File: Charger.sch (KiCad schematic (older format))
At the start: 47 parts, among them J1 Input, J2 USB-A-S-X-X-SM2, J3 USB-A-S-X-X-SM2, U1 LT1085-5.0, U2 TPS2546, U3 LT3798MPMSETRPBF, U4 TPS2546RTER

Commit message: schematics completed
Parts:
- removed D? (x2): D, symbol Device:D
- removed TR1: TEZ6.0-D-1, Transformer_THT:Transformer_Breve_TEZ-38x45, symbol Transformer:TEZ6.0-D-1
- removed U3: LT3798MPMSETRPBF, MSOP-16_MSE, symbol Charger-rescue:LT3798MPMSETRPBF-LT3798MPMSETRPBF
- added U3: LT3798MPMSETRPBF, MSOP-16_MSE, symbol LT3798MPMSETRPBF:LT3798MPMSETRPBF
- C6: renamed from C?; value C -> 4.7u
- R2: footprint R100k:RESC1005X40N -> (none)
- gave numbers to parts that had none: 28
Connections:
- net labels removed: +, -, DM, DP, Vout
- wire segments 103 -> 107
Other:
- moved on the sheet: D2

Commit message: Update Charger.sch
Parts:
- D4: value D_Zener -> DFLZ33
- D5: value DIODE -> GSD2004W-V
- M1: value MNMOS -> BSC42DN25NS3
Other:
- moved on the sheet: J2, J3
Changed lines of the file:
@@
 L Charger-rescue:USB-A-S-X-X-SM2-USB-A-S-X-X-SM2 J2
 U 1 1 6032BA44
-P 9500 1450
-F 0 "J2" H 9730 1446 50  0000 L CNN
-F 1 "USB-A-S-X-X-SM2" H 9730 1355 50  0000 L CNN
-F 2 "USB:SAMTEC_USB-A-S-X-X-SM2" H 9500 1450 50  0001 L BNN
-F 3 "" H 9500 1450 50  0001 L BNN
-F 4 "7.8 mm" H 9500 1450 50  0001 L BNN "MAXIMUM_PACKAGE_HEIGHT"
-F 5 "T" H 9500 1450 50  0001 L BNN "PARTREV"
-F 6 "Manufacturer Recommendations" H 9500 1450 50  0001 L BNN "STANDARD"
-F 7 "Samtec" H 9500 1450 50  0001 L BNN "MANUFACTURER"
-	1    9500 1450
+P 9600 1000
+F 0 "J2" H 9830 996 50  0000 L CNN
+F 1 "USB-A-S-X-X-SM2" H 9830 905 50  0000 L CNN
+F 2 "USB:SAMTEC_USB-A-S-X-X-SM2" H 9600 1000 50  0001 L BNN
+F 3 "" H 9600 1000 50  0001 L BNN
+F 4 "7.8 mm" H 9600 1000 50  0001 L BNN "MAXIMUM_PACKAGE_HEIGHT"
+F 5 "T" H 9600 1000 50  0001 L BNN "PARTREV"
+F 6 "Manufacturer Recommendations" H 9600 1000 50  0001 L BNN "STANDARD"
+F 7 "Samtec" H 9600 1000 50  0001 L BNN "MANUFACTURER"
+	1    9600 1000
 	1    0    0    -1
 $EndComp
 Text GLabel 6600 4300 3    50   Input ~ 0
 gnd
-Text GLabel 9100 1250 0    50   Input ~ 0
+Text GLabel 9200 800  0    50   Input ~ 0
 Vout1
-Text GLabel 9100 1550 0    50   Input ~ 0
+Text GLabel 9200 1100 0    50   Input ~ 0
 gnd
 $Comp
@@
 	1    0    0    -1
 $EndComp
-Text GLabel 9100 1350 0    50   Input ~ 0
+Text GLabel 9200 900  0    50   Input ~ 0
 DM1
-Text GLabel 9100 1450 0    50   Input ~ 0
+Text GLabel 9200 1000 0    50   Input ~ 0
 DP1
 Text GLabel 8650 2550 2    50   Input ~ 0
@@
 L Charger-rescue:USB-A-S-X-X-SM2-USB-A-S-X-X-SM2 J3
 U 1 1 60370EEE
-P 9900 4750
-F 0 "J3" H 10130 4746 50  0000 L CNN
-F 1 "USB-A-S-X-X-SM2" H 10130 4655 50  0000 L CNN
-F 2 "SAMTEC_USB-A-S-X-X-SM2" H 9900 4750 50  0001 L BNN
-F 3 "" H 9900 4750 50  0001 L BNN
-F 4 "7.8 mm" H 9900 4750 50  0001 L BNN "MAXIMUM_PACKAGE_HEIGHT"
-F 5 "T" H 9900 4750 50  0001 L BNN "PARTREV"
-F 6 "Manufacturer Recommendations" H 9900 4750 50  0001 L BNN "STANDARD"
-F 7 "Samtec" H 9900 4750 50  0001 L BNN "MANUFACTURER"
-	1    9900 4750
-	1    0    0    -1
-$EndComp
-Text GLabel 9500 4850 0    50   Input ~ 0
-gnd
-Text GLabel 9500 4750 0    50   Input ~ 0
+P 7550 950
+F 0 "J3" H 7780 946 50  0000 L CNN
+F 1 "USB-A-S-X-X-SM2" H 7780 855 50  0000 L CNN
+F 2 "SAMTEC_USB-A-S-X-X-SM2" H 7550 950 50  0001 L BNN
+F 3 "" H 7550 950 50  0001 L BNN
+F 4 "7.8 mm" H 7550 950 50  0001 L BNN "MAXIMUM_PACKAGE_HEIGHT"
+F 5 "T" H 7550 950 50  0001 L BNN "PARTREV"
+F 6 "Manufacturer Recommendations" H 7550 950 50  0001 L BNN "STANDARD"
+F 7 "Samtec" H 7550 950 50  0001 L BNN "MANUFACTURER"
+	1    7550 950
+	1    0    0    -1
+$EndComp
+Text GLabel 7150 1050 0    50   Input ~ 0
+gnd
+Text GLabel 7150 950  0    50   Input ~ 0
 DP2
-Text GLabel 9500 4650 0    50   Input ~ 0
+Text GLabel 7150 850  0    50   Input ~ 0
 DM2
-Text GLabel 9500 4550 0    50   Input ~ 0
+Text GLabel 7150 750  0    50   Input ~ 0
 Vout2
 Text GLabel 8600 4650 2    50   Input ~ 0
@@
 P 5650 5850
 F 0 "M1" H 5938 5896 50  0000 L CNN
-F 1 "MNMOS" H 5938 5805 50  0000 L CNN
+F 1 "BSC42DN25NS3" H 5938 5805 50  0000 L CNN
 F 2 "" H 5625 5850 50  0001 C CNN
 F 3 "~" H 5625 5850 50  0001 C CNN
@@
 P 4600 4700
 F 0 "D5" V 4646 4572 50  0000 R CNN
-F 1 "DIODE" V 4555 4572 50  0000 R CNN
+F 1 "GSD2004W-V" V 4555 4572 50  0000 R CNN
 F 2 "" H 4600 4700 50  0001 C CNN
 F 3 "~" H 4600 4700 50  0001 C CNN
@@
 P 4600 4050
 F 0 "D4" V 4646 3970 50  0000 R CNN
-F 1 "D_Zener" V 4555 3970 50  0000 R CNN
+F 1 "DFLZ33" V 4555 3970 50  0000 R CNN
 F 2 "" H 4600 4050 50  0001 C CNN
 F 3 "~" H 4600 4050 50  0001 C CNN
@@
 L power:PWR_FLAG #FLG0102
 U 1 1 60397240
-P 9100 1550
-F 0 "#FLG0102" H 9100 1625 50  0001 C CNN
-F 1 "PWR_FLAG" H 9100 1723 50  0000 C CNN
-F 2 "" H 9100 1550 50  0001 C CNN
-F 3 "~" H 9100 1550 50  0001 C CNN
-	1    9100 1550
+P 9200 1100
+F 0 "#FLG0102" H 9200 1175 50  0001 C CNN
+F 1 "PWR_FLAG" H 9200 1273 50  0000 C CNN
+F 2 "" H 9200 1100 50  0001 C CNN
+F 3 "~" H 9200 1100 50  0001 C CNN
+	1    9200 1100
 	-1   0    0    1
 $EndComp

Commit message: footprint added
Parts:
- removed D3: 1N4148, symbol Charger-rescue:1N4148-1N4148
- removed L1, L2, L3: L, symbol Device:L
- removed M1: BSC42DN25NS3, symbol pspice:MNMOS
- added D3: 1N4148WS, 1N4148WS:SODFL2512X100N, symbol 1N4148WS:1N4148WS
- added Q1: BSC42DN25NS3, MOSFET:SOT230P700X180-4N, symbol FQT4N25TF:FQT4N25TF
- added TR1: Wuerth_750343373, Transformer_THT:Transformer_Wuerth_750343373, symbol Transformer:Wuerth_750343373
- C1: footprint (none) -> Capacitor_THT:CP_Radial_D10.0mm_P7.50mm
- C2, C6: footprint (none) -> cap4:CAPC2012X140N
- C4, C5, C7, C9: footprint (none) -> Capacitor_THT:CP_Radial_D4.0mm_P1.50mm
- C8: footprint (none) -> Capacitor_THT:CP_Radial_D8.0mm_P3.80mm
- D2: footprint DIOAD1060W80L520D270 -> 1N4007:DIOAD1060W80L520D270
- D4, D5: footprint (none) -> 1N4148WS:SODFL2512X100N
- D6: value D -> MBRS360; footprint (none) -> 1N4148WS:SODFL2512X100N
- J3: footprint SAMTEC_USB-A-S-X-X-SM2 -> USB:SAMTEC_USB-A-S-X-X-SM2
- R1, R12, R14, R2: footprint (none) -> R100k:RESC1005X40N
- R10, R16, R5, R8: footprint (none) -> R806:RESC5025X70N
- R11, R13: footprint (none) -> R1Meg:RESC2012X65N
- R15, R18: footprint (none) -> R20:RESC1005X35N
- R17, R6, R7, R9: footprint (none) -> R169:RESC1608X50N
- U3: footprint MSOP-16_MSE -> LT3798:MSOP-16_MSE
- U4: footprint RTE0016C -> footprints:TPS2546RTER

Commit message: transformer footprint added
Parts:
- removed TR1: Wuerth_750343373, Transformer_THT:Transformer_Wuerth_750343373, symbol Transformer:Wuerth_750343373
- added T1: 760875131, 760875131:760875131, symbol 760875131:760875131
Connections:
- net labels added: Vsmp
- wire segments 107 -> 108
- no-connect marks 8 -> 12
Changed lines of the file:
@@
 Text GLabel 4600 5950 2    50   Input ~ 0
 gnd
-Wire Wire Line
-	6300 4300 6600 4300
 Connection ~ 6600 4300
 Text GLabel 4600 6050 2    50   Input ~ 0
@@
 U 1 1 603824E5
 P 4600 4700
-F 0 "D5" V 4646 4572 50  0000 R CNN
-F 1 "GSD2004W-V" V 4555 4572 50  0000 R CNN
+F 0 "D5" V 4600 5000 50  0000 R CNN
+F 1 "GSD2004W-V" V 4500 5350 50  0000 R CNN
 F 2 "1N4148WS:SODFL2512X100N" H 4600 4700 50  0001 C CNN
 F 3 "~" H 4600 4700 50  0001 C CNN
@@
 U 1 1 60384E6B
 P 4600 4050
-F 0 "D4" V 4646 3970 50  0000 R CNN
-F 1 "DFLZ33" V 4555 3970 50  0000 R CNN
+F 0 "D4" V 4650 4350 50  0000 R CNN
+F 1 "DFLZ33" V 4550 4500 50  0000 R CNN
 F 2 "1N4148WS:SODFL2512X100N" H 4600 4050 50  0001 C CNN
 F 3 "~" H 4600 4050 50  0001 C CNN
@@
 Wire Wire Line
 	2600 2100 4600 2100
-Wire Wire Line
-	4600 2100 4600 3550
 Connection ~ 2600 2100
-Wire Wire Line
-	4600 5050 5250 5050
-Connection ~ 5250 5050
-Wire Wire Line
-	5250 5050 5750 5050
-Text GLabel 5250 3450 0    50   Input ~ 0
-gnd
 Text GLabel 3950 3150 3    50   Input ~ 0
 dcm
@@
 	5950 2350 6000 2350
 Connection ~ 5950 2350
-Wire Wire Line
-	5650 2350 5650 3350
 Text GLabel 5950 3000 3    50   Input ~ 0
 gnd
@@
 	2750 3150 2950 3150
 $Comp
-L Transformer:Wuerth_750343373 TR1
-U 1 1 603B20C8
-P 5450 3550
-F 0 "TR1" H 5500 2900 50  0000 C CNN
-F 1 "Wuerth_750343373" H 5550 2800 50  0000 C CNN
-F 2 "Transformer_THT:Transformer_Wuerth_750343373" H 5450 3000 50  0001 C CNN
-F 3 "https://katalog.we-online.com/ctm/datasheet/750343373.pdf" H 5450 3550 50  0001 C CNN
-	1    5450 3550
-	-1   0    0    1
-$EndComp
-Wire Wire Line
-	3850 3150 5250 3150
-Wire Wire Line
-	5250 3550 4600 3550
-Connection ~ 4600 3550
-Wire Wire Line
-	4600 3550 4600 3900
-Wire Wire Line
-	5250 3850 5250 5050
-Text GLabel 5650 3750 2    50   Input ~ 0
-gnd
-$Comp
 L FQT4N25TF:FQT4N25TF Q1
 U 1 1 603D4489
@@
 Wire Wire Line
 	5750 5550 5750 5650
+Text GLabel 5650 2350 0    50   Input ~ 0
+Vsmp
+$Comp
+L 760875131:760875131 T1
+U 1 1 60386D1D
+P 6050 3900
+F 0 "T1" H 6600 3135 50  0000 C CNN
+F 1 "760875131" H 6600 3226 50  0000 C CNN
+F 2 "760875131:760875131" H 7000 4000 50  0001 L CNN
+F 3 "https://katalog.we-online.de/pbs/datasheet/760875131.pdf" H 7000 3900 50  0001 L CNN
+F 4 "Audio Transformers / Signal Transformers WE-UOST Univ Offline 1500uH 0.8A 140mOhm" H 7000 3800 50  0001 L CNN "Description"
+F 5 "14" H 7000 3700 50  0001 L CNN "Height"
+F 6 "Wurth Elektronik" H 7000 3600 50  0001 L CNN "Manufacturer_Name"
+F 7 "760875131" H 7000 3500 50  0001 L CNN "Manufacturer_Part_Number"
+F 8 "710-760875131" H 7000 3400 50  0001 L CNN "Mouser Part Number"
+F 9 "https://www.mouser.co.uk/ProductDetail/Wurth-Elektronik/760875131?qs=TB%2FQ0sBK%2FGdsHNIF9xNITw%3D%3D" H 7000 3300 50  0001 L CNN "Mouser Price/Stock"
+F 10 "" H 7000 3200 50  0001 L CNN "Arrow Part Number"
+F 11 "" H 7000 3100 50  0001 L CNN "Arrow Price/Stock"
+	1    6050 3900
+	-1   0    0    1
+$EndComp
+Wire Wire Line
+	4600 2100 4600 3900
+Wire Wire Line
+	4600 5050 4900 5050
+Wire Wire Line
+	6300 4300 6600 4300
+Text GLabel 6050 3600 2    50   Input ~ 0
+gnd
+Text GLabel 6050 3400 2    50   Input ~ 0
+gnd
+Wire Wire Line
+	3850 3150 4100 3150
+Wire Wire Line
+	4100 3150 4100 3600
+Wire Wire Line
+	4100 3600 4950 3600
+Text GLabel 4950 3400 0    50   Input ~ 0
+gnd
+Wire Wire Line
+	4950 3900 4600 3900
+Connection ~ 4600 3900
+Wire Wire Line
+	4950 3800 4900 3800
+Wire Wire Line
+	4900 3800 4900 5050
+Connection ~ 4900 5050
+Wire Wire Line
+	4900 5050 5750 5050
+Text GLabel 6050 3900 2    50   Input ~ 0
+Vsmp
+Text GLabel 6050 3700 2    50   Input ~ 0
+Vsmp
+NoConn ~ 4950 3500
+NoConn ~ 4950 3700
+NoConn ~ 6050 3800
+NoConn ~ 6050 3500
 $EndSCHEMATC

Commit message: footprints finalised
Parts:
- D4, D5, D6: footprint 1N4148WS:SODFL2512X100N -> Diode_SMD:D_1812_4532Metric_Pad1.30x3.40mm_HandSolder
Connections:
- no-connect marks 12 -> 13
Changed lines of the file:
@@
 F 0 "D5" V 4600 5000 50  0000 R CNN
 F 1 "GSD2004W-V" V 4500 5350 50  0000 R CNN
-F 2 "1N4148WS:SODFL2512X100N" H 4600 4700 50  0001 C CNN
+F 2 "Diode_SMD:D_1812_4532Metric_Pad1.30x3.40mm_HandSolder" H 4600 4700 50  0001 C CNN
 F 3 "~" H 4600 4700 50  0001 C CNN
 	1    4600 4700
@@
 F 0 "D4" V 4650 4350 50  0000 R CNN
 F 1 "DFLZ33" V 4550 4500 50  0000 R CNN
-F 2 "1N4148WS:SODFL2512X100N" H 4600 4050 50  0001 C CNN
+F 2 "Diode_SMD:D_1812_4532Metric_Pad1.30x3.40mm_HandSolder" H 4600 4050 50  0001 C CNN
 F 3 "~" H 4600 4050 50  0001 C CNN
 	1    4600 4050
@@
 F 0 "D6" H 5800 2133 50  0000 C CNN
 F 1 "MBRS360" H 5800 2224 50  0000 C CNN
-F 2 "1N4148WS:SODFL2512X100N" H 5800 2350 50  0001 C CNN
+F 2 "Diode_SMD:D_1812_4532Metric_Pad1.30x3.40mm_HandSolder" H 5800 2350 50  0001 C CNN
 F 3 "~" H 5800 2350 50  0001 C CNN
 	1    5800 2350
@@
 NoConn ~ 6050 3800
 NoConn ~ 6050 3500
+NoConn ~ 5450 -750
 $EndSCHEMATC

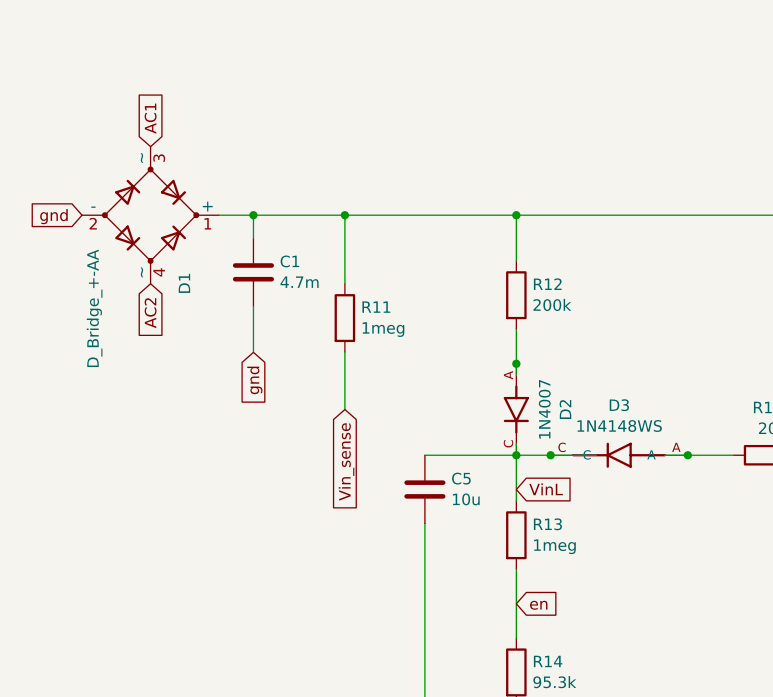
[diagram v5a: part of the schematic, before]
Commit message: added fuse
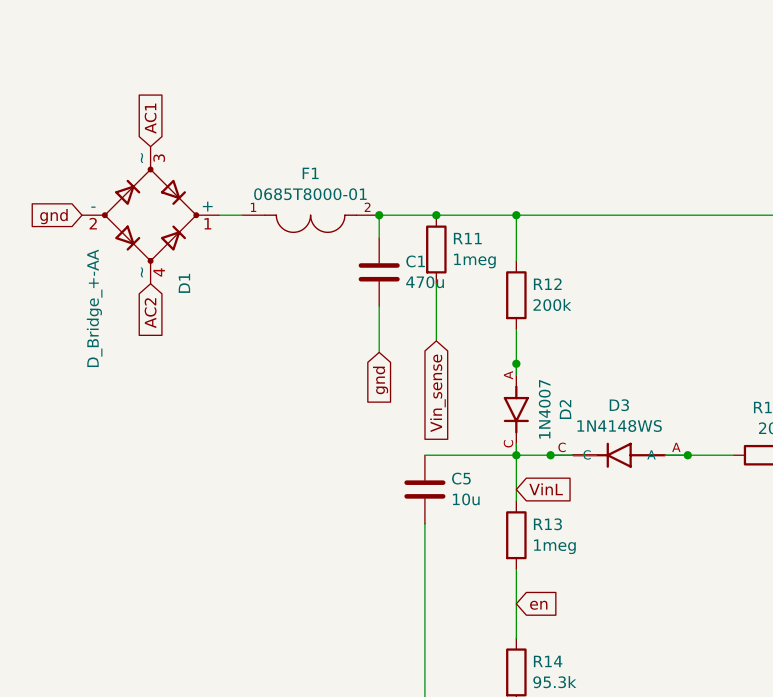
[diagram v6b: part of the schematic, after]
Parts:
- added F1: 0685T8000-01, fuse:FUSC3215X83N, symbol 0685T8000-01:0685T8000-01
- C1: value 4.7m -> 470u
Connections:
- wire segments 108 -> 107
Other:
- moved on the sheet: C1, R11
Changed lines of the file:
@@
 L Device:C C1
 U 1 1 6039DE55
-P 1450 2350
-F 0 "C1" H 1565 2396 50  0000 L CNN
-F 1 "4.7m" H 1565 2305 50  0000 L CNN
-F 2 "Capacitor_THT:CP_Radial_D10.0mm_P7.50mm" H 1488 2200 50  0001 C CNN
-F 3 "~" H 1450 2350 50  0001 C CNN
-	1    1450 2350
-	1    0    0    -1
-$EndComp
-Text GLabel 1450 2700 3    50   Input ~ 0
-gnd
-Wire Wire Line
-	1300 2100 1450 2100
-Wire Wire Line
-	1450 2100 1450 2200
-Wire Wire Line
-	1450 2500 1450 2700
-Connection ~ 1450 2100
+P 2000 2350
+F 0 "C1" H 2115 2396 50  0000 L CNN
+F 1 "470u" H 2115 2305 50  0000 L CNN
+F 2 "Capacitor_THT:CP_Radial_D10.0mm_P7.50mm" H 2038 2200 50  0001 C CNN
+F 3 "~" H 2000 2350 50  0001 C CNN
+	1    2000 2350
+	1    0    0    -1
+$EndComp
+Text GLabel 2000 2700 3    50   Input ~ 0
+gnd
+Wire Wire Line
+	2000 2100 2000 2200
+Wire Wire Line
+	2000 2500 2000 2700
 $Comp
 L Device:R R11
 U 1 1 603A25C6
-P 1850 2550
-F 0 "R11" H 1920 2596 50  0000 L CNN
-F 1 "1meg" H 1920 2505 50  0000 L CNN
-F 2 "R1Meg:RESC2012X65N" V 1780 2550 50  0001 C CNN
-F 3 "~" H 1850 2550 50  0001 C CNN
-	1    1850 2550
-	1    0    0    -1
-$EndComp
-Text GLabel 1850 2950 3    50   Input ~ 0
+P 2250 2250
+F 0 "R11" H 2320 2296 50  0000 L CNN
+F 1 "1meg" H 2320 2205 50  0000 L CNN
+F 2 "R1Meg:RESC2012X65N" V 2180 2250 50  0001 C CNN
+F 3 "~" H 2250 2250 50  0001 C CNN
+	1    2250 2250
+	1    0    0    -1
+$EndComp
+Text GLabel 2250 2650 3    50   Input ~ 0
 Vin_sense
 Wire Wire Line
-	1850 2100 1850 2400
-Wire Wire Line
-	1850 2700 1850 2950
-Connection ~ 1850 2100
-Wire Wire Line
-	1850 2100 1450 2100
+	2250 2400 2250 2650
 $Comp
 L Device:R R12
@@
 	2600 3100 2600 3150
 Wire Wire Line
-	2600 2100 1850 2100
+	2600 2100 2250 2100
 Wire Wire Line
 	2200 3150 2600 3150
@@
 NoConn ~ 6050 3500
 NoConn ~ 5450 -750
+Connection ~ 2250 2100
+Connection ~ 2000 2100
+Wire Wire Line
+	2000 2100 2250 2100
+Wire Wire Line
+	1300 2100 1400 2100
+$Comp
+L 0685T8000-01:0685T8000-01 F1
+U 1 1 603AA530
+P 1700 2100
+F 0 "F1" H 1700 2281 50  0000 C CNN
+F 1 "0685T8000-01" H 1700 2190 50  0000 C CNN
+F 2 "fuse:FUSC3215X83N" H 1700 2100 50  0001 L BNN
+F 3 "" H 1700 2100 50  0001 L BNN
+F 4 "0.83mm" H 1700 2100 50  0001 L BNN "MAXIMUM_PACKAGE_HEIGHT"
+F 5 "IPC-7351B" H 1700 2100 50  0001 L BNN "STANDARD"
+F 6 "BELFUSE" H 1700 2100 50  0001 L BNN "MANUFACTURER"
+F 7 "Jan2019" H 1700 2100 50  0001 L BNN "PARTREV"
+	1    1700 2100
+	1    0    0    -1
+$EndComp
 $EndSCHEMATC

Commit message: compact
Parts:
- removed J1: Input, TerminalBlock:TerminalBlock_bornier-2_P5.08mm, symbol Connector:Screw_Terminal_01x02
- added TP1, TP2: TestPoint, TestPoint:TestPoint_Pad_2.0x2.0mm, symbol Connector:TestPoint
- C1: footprint Capacitor_THT:CP_Radial_D10.0mm_P7.50mm -> Capacitor_SMD:CP_Elec_5x4.4
- C3: footprint Capacitor_SMD:CP_Elec_3x5.3 -> Capacitor_SMD:CP_Elec_4x3.9
- C4, C5, C7, C9: footprint Capacitor_THT:CP_Radial_D4.0mm_P1.50mm -> Capacitor_SMD:CP_Elec_3x5.3
- C8: footprint Capacitor_THT:CP_Radial_D8.0mm_P3.80mm -> Capacitor_SMD:CP_Elec_5x4.4
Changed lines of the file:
@@
 F 0 "C3" H 6778 3296 50  0000 L CNN
 F 1 "47u" H 6778 3205 50  0000 L CNN
-F 2 "Capacitor_SMD:CP_Elec_3x5.3" H 6600 3250 50  0001 C CNN
+F 2 "Capacitor_SMD:CP_Elec_4x3.9" H 6600 3250 50  0001 C CNN
 F 3 "~" H 6600 3250 50  0001 C CNN
 	1    6600 3250
-	1    0    0    -1
-$EndComp
-$Comp
-L Connector:Screw_Terminal_01x02 J1
-U 1 1 6031590C
-P 3600 700
-F 0 "J1" H 3680 692 50  0000 L CNN
-F 1 "Input" H 3680 601 50  0000 L CNN
-F 2 "TerminalBlock:TerminalBlock_bornier-2_P5.08mm" H 3600 700 50  0001 C CNN
-F 3 "~" H 3600 700 50  0001 C CNN
-	1    3600 700
 	1    0    0    -1
 $EndComp
@@
 NoConn ~ 7250 3250
 NoConn ~ 8650 3850
-Text GLabel 3400 700  0    50   Input ~ 0
+Text GLabel 3800 750  2    50   Input ~ 0
 AC1
-Text GLabel 3400 800  0    50   Input ~ 0
+Text GLabel 3800 850  2    50   Input ~ 0
 AC2
 Wire Wire Line
@@
 F 0 "C4" H 1928 7196 50  0000 L CNN
 F 1 "0.1u" H 1928 7105 50  0000 L CNN
-F 2 "Capacitor_THT:CP_Radial_D4.0mm_P1.50mm" H 1750 7150 50  0001 C CNN
+F 2 "Capacitor_SMD:CP_Elec_3x5.3" H 1750 7150 50  0001 C CNN
 F 3 "~" H 1750 7150 50  0001 C CNN
 	1    1750 7150
@@
 F 0 "C9" H 6115 7346 50  0000 L CNN
 F 1 "22p" H 6115 7255 50  0000 L CNN
-F 2 "Capacitor_THT:CP_Radial_D4.0mm_P1.50mm" H 6038 7150 50  0001 C CNN
+F 2 "Capacitor_SMD:CP_Elec_3x5.3" H 6038 7150 50  0001 C CNN
 F 3 "~" H 6000 7300 50  0001 C CNN
 	1    6000 7300
@@
 F 0 "C1" H 2115 2396 50  0000 L CNN
 F 1 "470u" H 2115 2305 50  0000 L CNN
-F 2 "Capacitor_THT:CP_Radial_D10.0mm_P7.50mm" H 2038 2200 50  0001 C CNN
+F 2 "Capacitor_SMD:CP_Elec_5x4.4" H 2038 2200 50  0001 C CNN
 F 3 "~" H 2000 2350 50  0001 C CNN
 	1    2000 2350
@@
 F 0 "C5" H 2315 3346 50  0000 L CNN
 F 1 "10u" H 2315 3255 50  0000 L CNN
-F 2 "Capacitor_THT:CP_Radial_D4.0mm_P1.50mm" H 2238 3150 50  0001 C CNN
+F 2 "Capacitor_SMD:CP_Elec_3x5.3" H 2238 3150 50  0001 C CNN
 F 3 "~" H 2200 3300 50  0001 C CNN
 	1    2200 3300
@@
 F 0 "C7" V 4948 6950 50  0000 C CNN
 F 1 "4.7p" V 5039 6950 50  0000 C CNN
-F 2 "Capacitor_THT:CP_Radial_D4.0mm_P1.50mm" H 5238 6800 50  0001 C CNN
+F 2 "Capacitor_SMD:CP_Elec_3x5.3" H 5238 6800 50  0001 C CNN
 F 3 "~" H 5200 6950 50  0001 C CNN
 	1    5200 6950
@@
 F 0 "C8" H 6065 2896 50  0000 L CNN
 F 1 "470u" H 6065 2805 50  0000 L CNN
-F 2 "Capacitor_THT:CP_Radial_D8.0mm_P3.80mm" H 5988 2700 50  0001 C CNN
+F 2 "Capacitor_SMD:CP_Elec_5x4.4" H 5988 2700 50  0001 C CNN
 F 3 "~" H 5950 2850 50  0001 C CNN
 	1    5950 2850
@@
 	1    0    0    -1
 $EndComp
+$Comp
+L Connector:TestPoint TP1
+U 1 1 603D66F1
+P 3800 750
+F 0 "TP1" V 3995 822 50  0000 C CNN
+F 1 "TestPoint" V 3904 822 50  0000 C CNN
+F 2 "TestPoint:TestPoint_Pad_2.0x2.0mm" H 4000 750 50  0001 C CNN
+F 3 "~" H 4000 750 50  0001 C CNN
+	1    3800 750
+	0    -1   -1   0
+$EndComp
+$Comp
+L Connector:TestPoint TP2
+U 1 1 603D7132
+P 3800 850
+F 0 "TP2" V 3600 1000 50  0000 C CNN
+F 1 "TestPoint" V 3700 1000 50  0000 C CNN
+F 2 "TestPoint:TestPoint_Pad_2.0x2.0mm" H 4000 850 50  0001 C CNN
+F 3 "~" H 4000 850 50  0001 C CNN
+	1    3800 850
+	0    -1   -1   0
+$EndComp
 $EndSCHEMATC
